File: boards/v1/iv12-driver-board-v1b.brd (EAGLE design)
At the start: 165.7 x 38.1 mm, 84 parts, among them J1 85791-4020, J2 SSW-106-02-S-S, J4 SSW-103-02-S-S, J5 SSW-106-02-S-S, Q1 BSS123, U2 HCPL-181-000E, U3 PIC18F67J60-I/PT, U4 25AA02E48T-I/OT

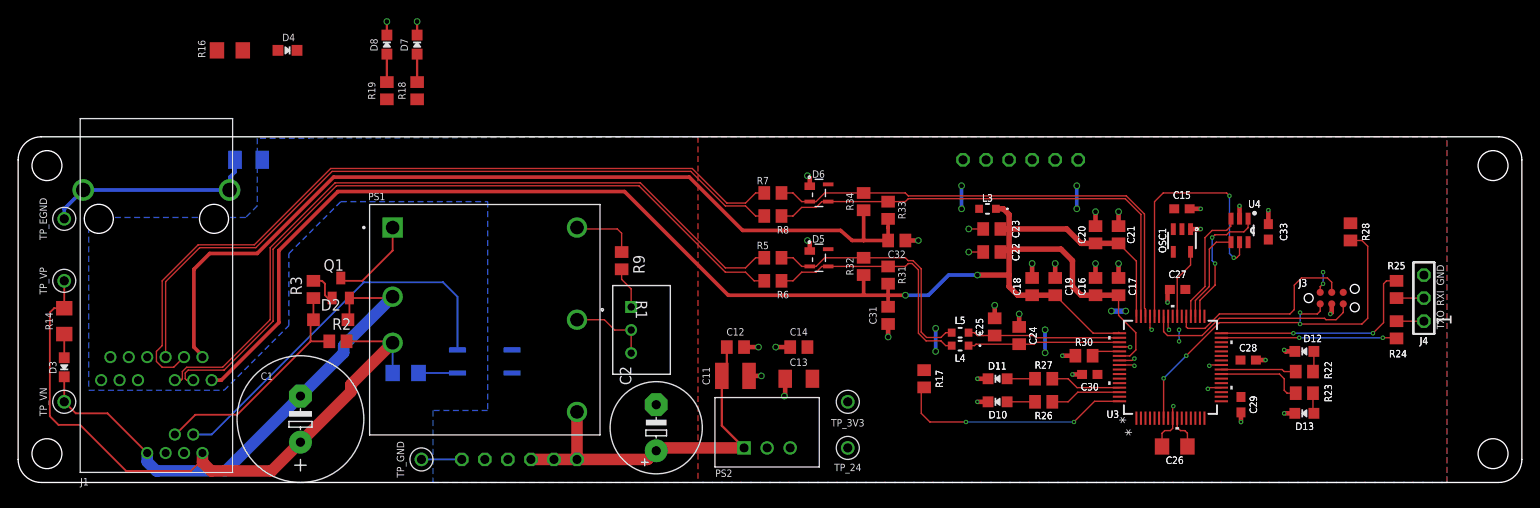
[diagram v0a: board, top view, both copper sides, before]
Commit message: changed to correct version of board
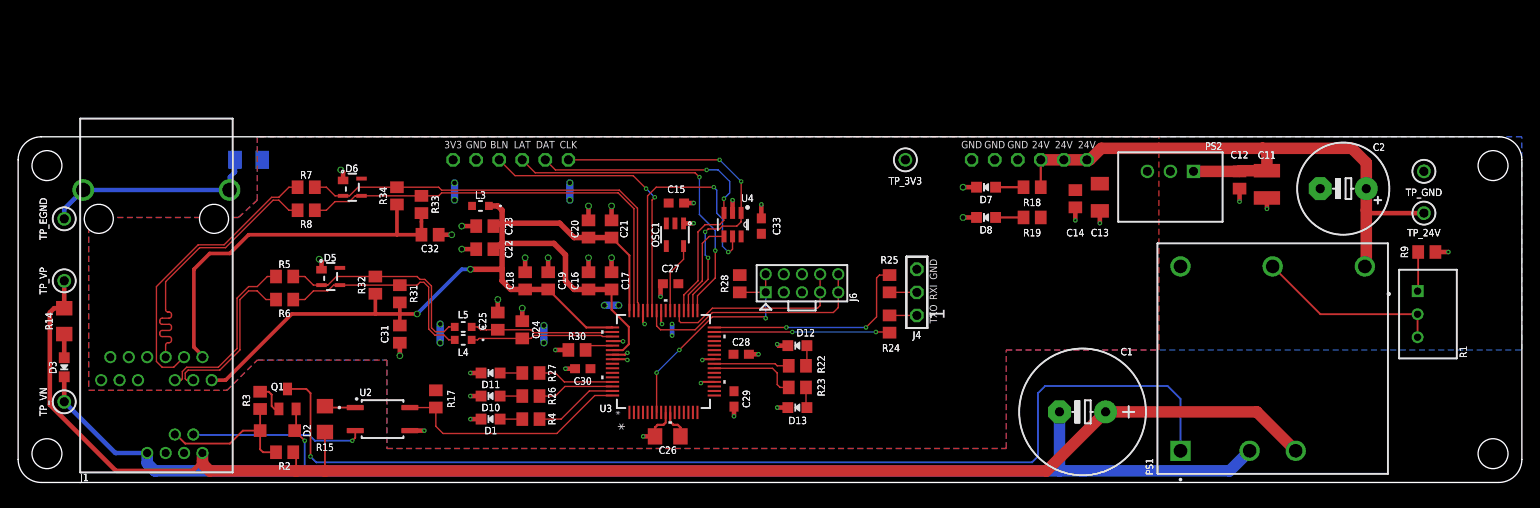
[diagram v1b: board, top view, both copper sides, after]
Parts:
- removed D4: RED, microbuilder:CHIPLED_0805_NOOUTLINE
- removed J3: (no value), tag-connect:TC2030-MCP-NL
- removed R16: 27k 1/4w, rcl:R1206
- removed TP_24: KEYSTONE_500X, 0GlenConnectors:KEYSTONE_TP500X
- added D1: RED, microbuilder:CHIPLED_0805_NOOUTLINE
- added J6: MOLEX-87758-1016, 0GlenConnectors:CON-2MM-2X5
- added R4: 1k, rcl:R0805
- added TP_24V: KEYSTONE_500X, 0GlenConnectors:KEYSTONE_TP500X
- R9: value 1k 1/8w -> 51k 1/8w
- moved TP_GND 115.0 mm to (149.9, 34.3), turned to 270 degrees
- moved R9 88.7 mm to (150.2, 25.4), turned to 180 degrees
- moved PS1 86.9 mm to (133.2, 13.7), turned to 90 degrees
- moved R1 86.7 mm to (151.4, 16.0)
- moved C1 86.2 mm to (112.2, 7.78), turned to 180 degrees
- moved C2 80.2 mm to (141.0, 32.4), turned to 180 degrees
- moved R19 72.5 mm to (106.7, 29.2), turned to 180 degrees
- moved D8 68.7 mm to (101.6, 29.2), turned to 90 degrees
- moved R18 68.6 mm to (106.7, 32.5), turned to 180 degrees
- moved R28 67.6 mm to (74.5, 21.9)
- moved J2 65.2 mm to (106.4, 35.6)
- moved D7 64.6 mm to (101.6, 32.5), turned to 90 degrees
- moved C11 62.3 mm to (132.6, 32.9), turned to 270 degrees
- moved C12 58.5 mm to (129.5, 33.3), turned to 270 degrees
- moved PS2 58.2 mm to (124.5, 34.3), turned to 180 degrees
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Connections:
- net N$8 renamed VCAP
- removed net BLANK_3V3: J5.2
- removed net CLK_3V3: J5.5
- removed net DATA_3V3: J5.3
- removed net LATCH_3V3: J5.4
- removed net N$23: D4.A, R16.2
- removed net NEO_DOUT: U3.5
- removed net VPPIN: R16.1
- new net BLANK: J5.4, U3.43
- new net LATCH: J5.3, U3.33
- new net LED3: R27.2, U3.61
- new net N$1: D1.A, R4.1
- net +24V: now also TP_24V.1; no longer TP_24.1
- net +3V3: now also J5.6, J6.3, J6.4; no longer J3.2, J5.1
- net /MCLR: now also J6.1, J6.2; no longer J3.1
- net ATFLAG: no longer D4.C
- net GND: now also D1.C, J5.5, J6.5, J6.6; no longer J3.3, J5.6
- net LED1: now also R4.2, U3.63; no longer R26.2, U3.62
- net LED2: now also R26.2, U3.62; no longer R27.2, U3.61
- net MOSI: now also J5.2
- net PGC: now also J6.10, J6.9; no longer J3.5
- net PGD: now also J6.7, J6.8; no longer J3.4
- net SCK: now also J5.1
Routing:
- net /CDB: track 9.82 -> 119.7 mm, vias 0 -> 1
- net VMAIN_P: track 73.7 -> 168.2 mm
- net VMAIN_N: track 58.4 -> 152.0 mm, vias 0 -> 1
- net TD_CT: track 184.0 -> 114.2 mm
- net TD0P: track 82.9 -> 19.0 mm
- net TDON: track 83.4 -> 19.6 mm
- net RD_CT: track 99.4 -> 42.5 mm
- net TD1N: track 86.5 -> 32.1 mm
- net TD1P: track 81.4 -> 31.6 mm
- net LATCH: track 0.00 -> 36.6 mm, vias 0 -> 2
- net BLANK: track 0.00 -> 31.5 mm, vias 0 -> 2
- net +24V: track 41.6 -> 68.8 mm
- net MOSI: track 13.5 -> 38.6 mm, vias 0 -> 2
- net ATFLAG: track 42.6 -> 19.1 mm, vias 0 -> 1
- net SCK: track 14.9 -> 38.4 mm, vias 2 -> 4
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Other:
- board text added: "24V"
- board text added: "3V3"
- board text added: "BLN"
- board text added: "C1"
- board text added: "C11"
- board text added: "C12"
- board text added: "C13"
- board text added: "C14"
- board text added: "C2"
- board text added: "C31"
- board text added: "C32"
- board text added: "C6"
- board text added: "CLK"
- board text added: "D1"
- board text added: "D2"
- board text added: "D3"
- board text added: "D5"
- board text added: "D6"
- board text added: "D7"
- board text added: "D8"
- board text added: "DAT"
- board text added: "J1"
- board text added: "J2"
- board text added: "J5"
- board text added: "J6"
- board text added: "LAT"
- board text added: "PS1"
- board text added: "PS2"
- board text added: "Q1"
- board text added: "R1"
- board text added: "R14"
- board text added: "R15"
- board text added: "R18"
- board text added: "R19"
- board text added: "R2"
- board text added: "R3"
- board text added: "R31"
- board text added: "R32"
- board text added: "R33"
- board text added: "R34"
- board text added: "R4"
- board text added: "R5"
- board text added: "R6"
- board text added: "R7"
- board text added: "R8"
- board text added: "R9"
- board text added: "TP_24V"
- board text added: "TP_3V3"
- board text added: "TP_EGND"
- board text added: "TP_GND"
- board text added: "TP_VN"
- board text added: "TP_VP"
- board text added: "U2"
- board text removed: "J3"
